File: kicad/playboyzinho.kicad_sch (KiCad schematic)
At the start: 9 parts, among them SW1 SW_SPDT, U1 esp32-s3-pl, U2 (Tela 2.8) CR2013-MI2120, U4 (Amplificador) MAX98357A I2S

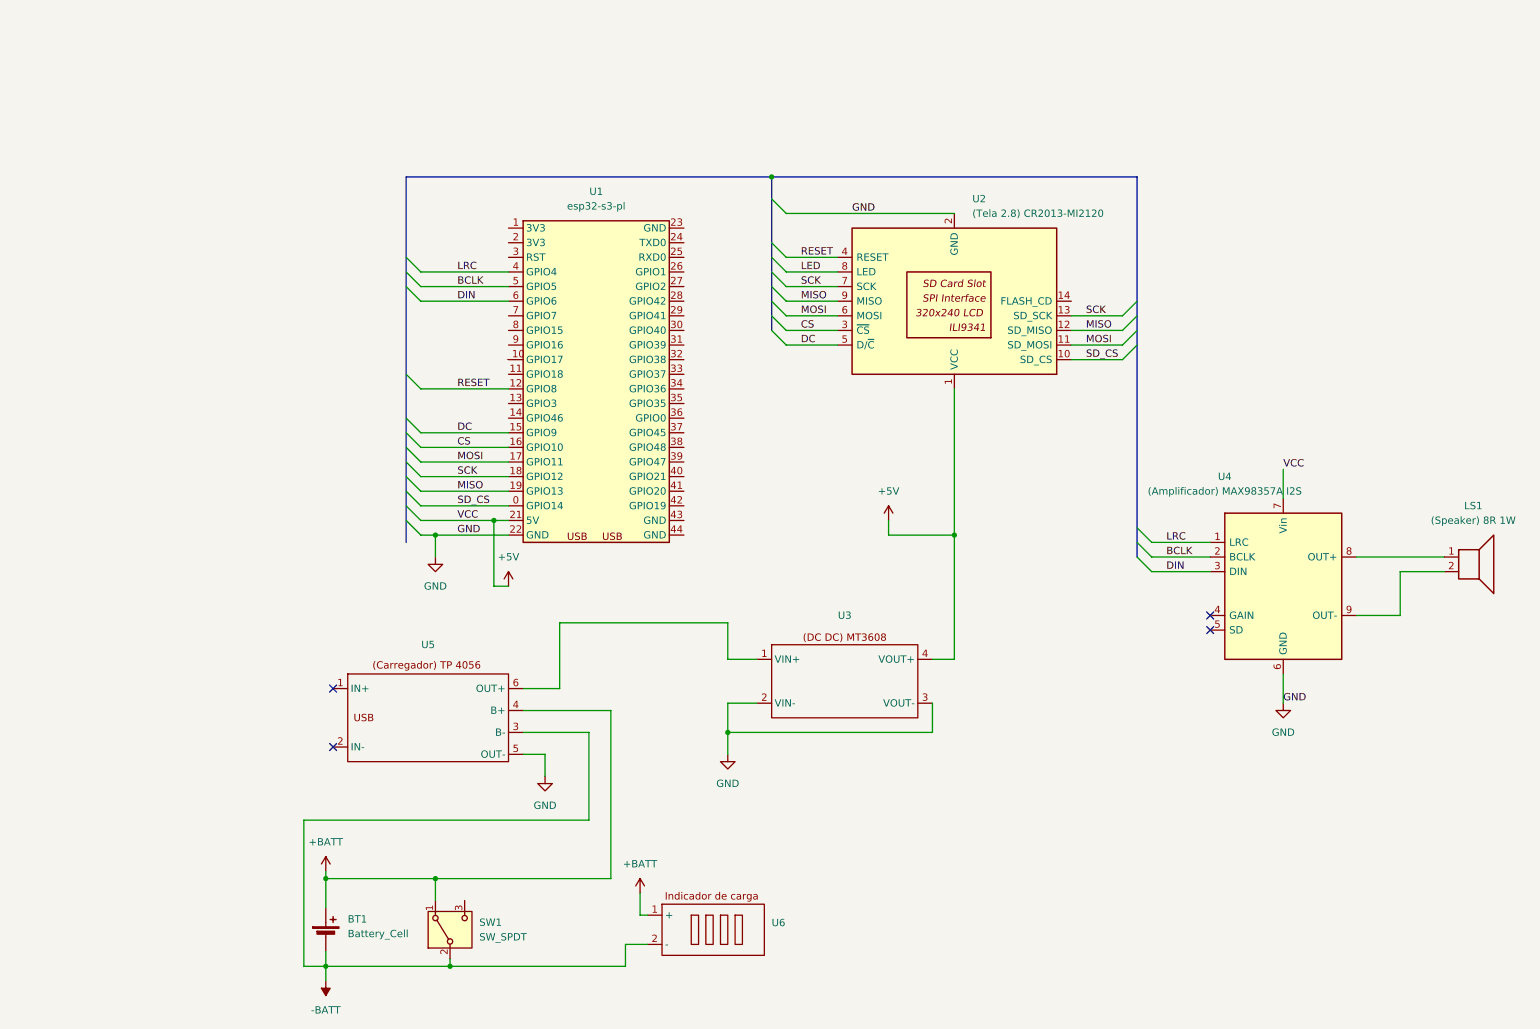
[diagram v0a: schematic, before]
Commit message: feat: adiciona lista de conexões, adiciona botões no esquemático, adiciona conexão LED que tava faltando no esquemático, remove imagens desnecessárias
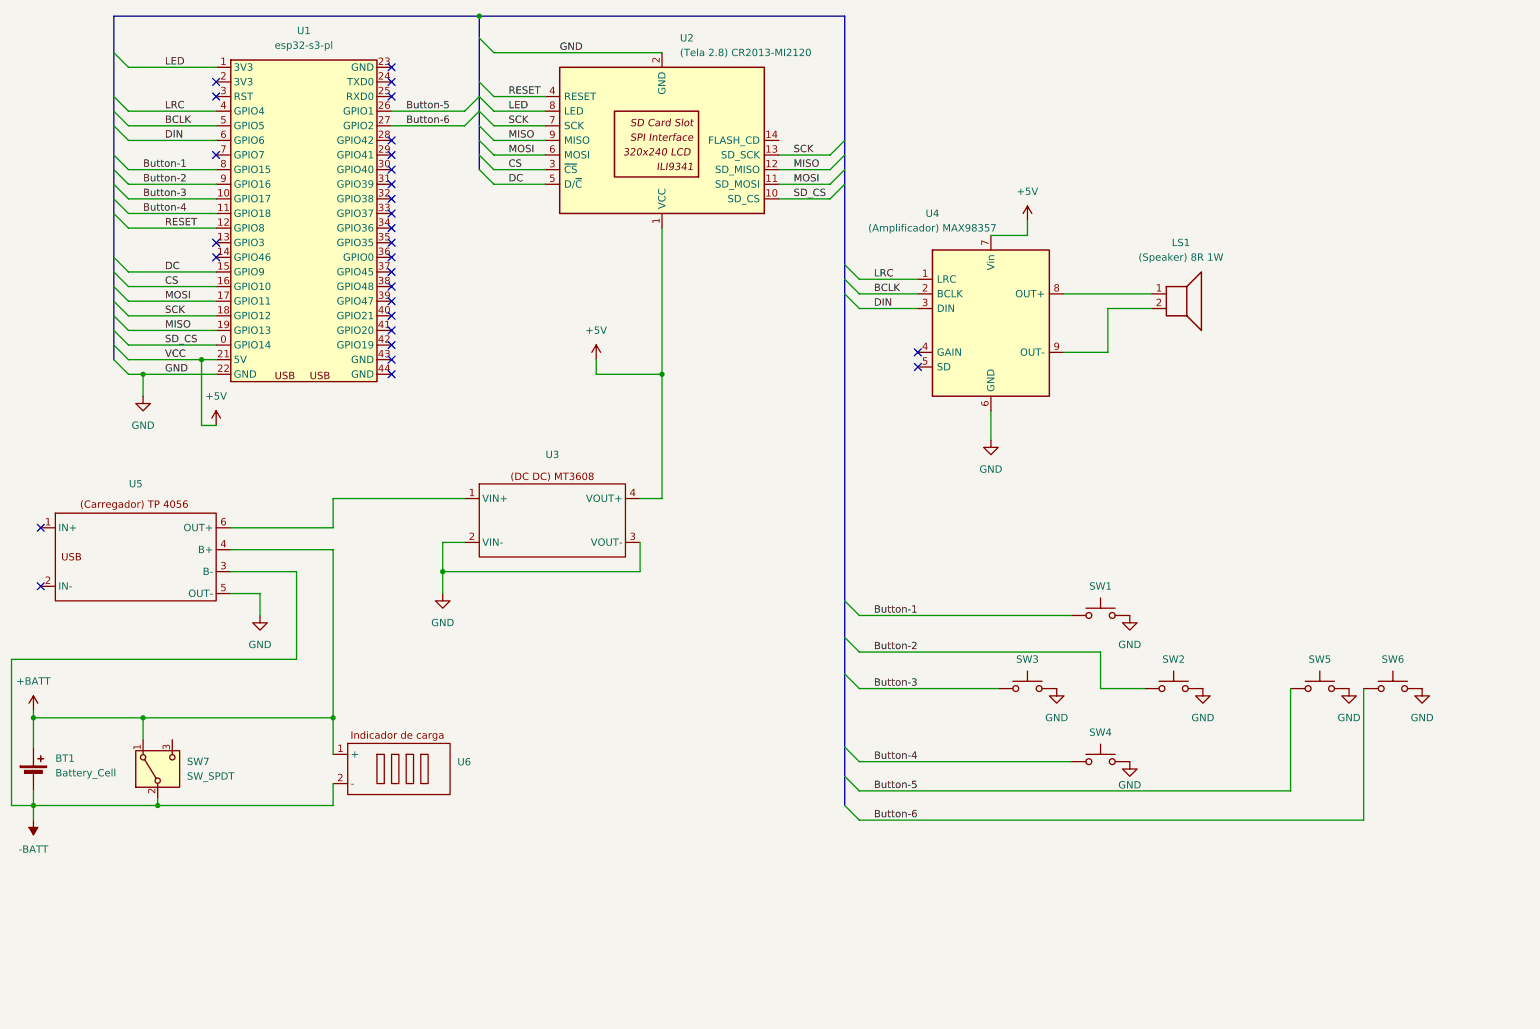
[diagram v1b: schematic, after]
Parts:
- added SW1, SW2, SW3, SW4, SW5, SW6: SW_Push, symbol Switch:SW_Push
- U4: value (Amplificador) MAX98357A I2S -> (Amplificador) MAX98357
- renumbered SW1 to SW7
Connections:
- net GND: now also SW1.2, SW2.2, SW3.2, SW4.2, SW5.2, SW6.2
- net LED: now also U1.1 (3V3)
- net Button-4: now reaches U1.11 (GPIO18)
- net Button-4: now also SW4.1
- net Button-5: now reaches U1.26 (GPIO1)
- net Button-5: now also SW5.1
- net Button-6: now reaches U1.27 (GPIO2)
- net Button-6: now also SW6.1
- net Button-1: now reaches U1.8 (GPIO15)
- net Button-1: now also SW1.1
- net Button-2: now reaches U1.9 (GPIO16)
- net Button-2: now also SW2.1
- new net Button-3: SW3.1, U1.10 (GPIO17)
- no-connect marks 4 -> 29
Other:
- moved on the sheet: BT1, LS1, SW7, U1, U2, U3, U4, U5, U6

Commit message: feat: cria novo símbolo para tela e adiciona ele no esquemático, finaliza o geralzão dos footprints (talvez precise de ajustes)
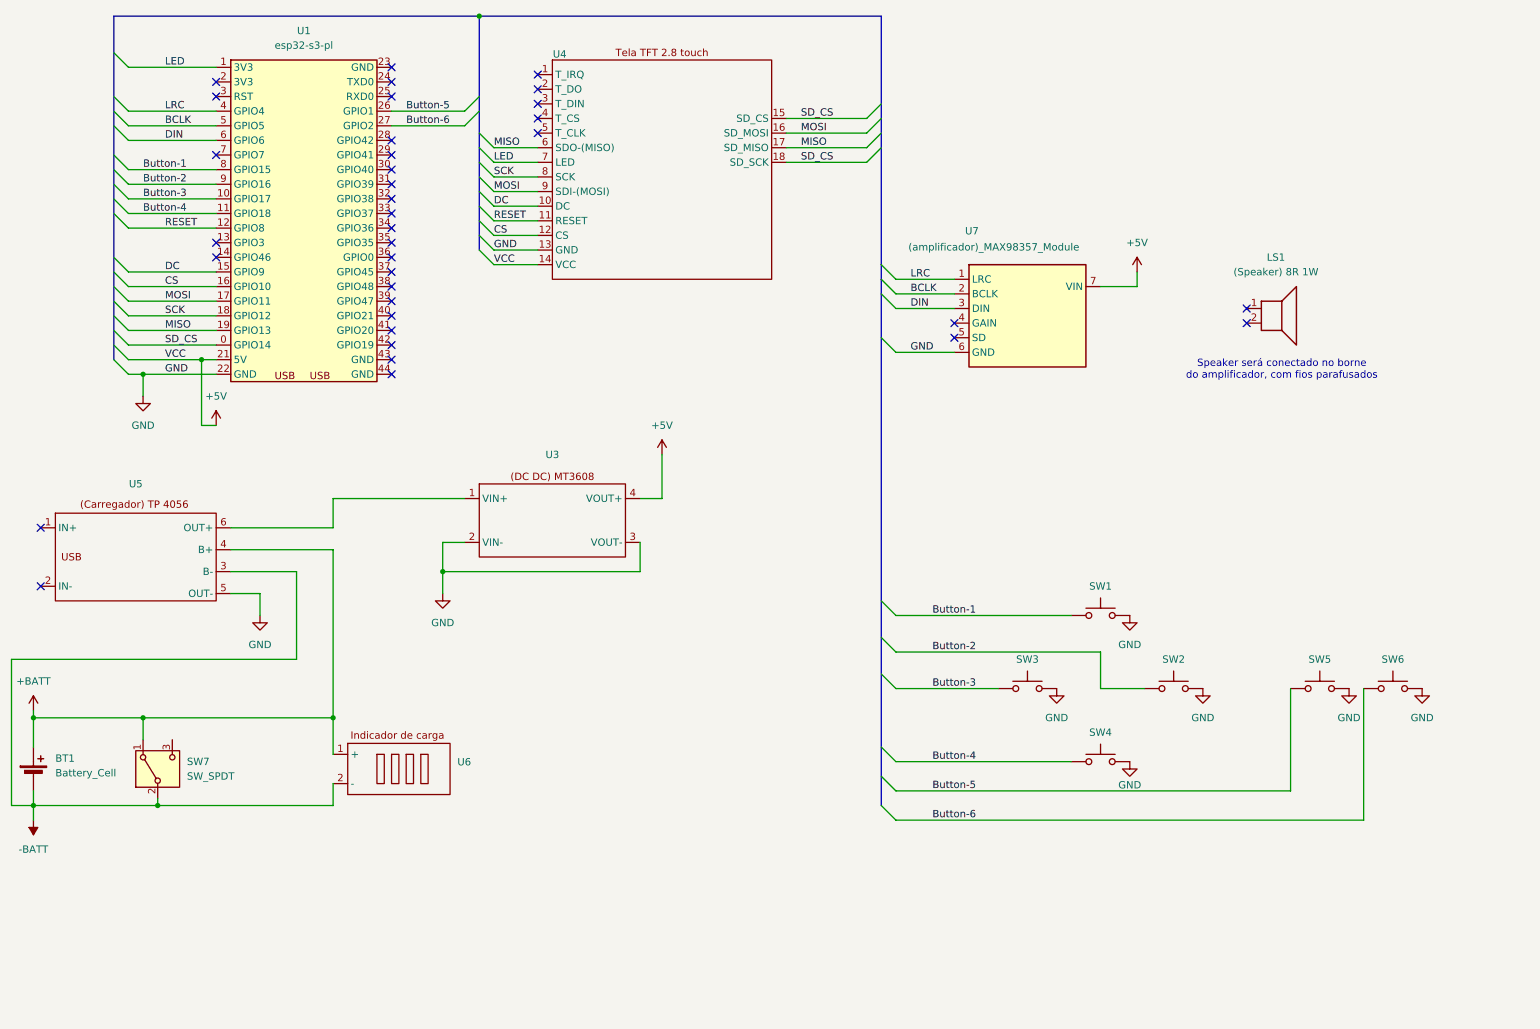
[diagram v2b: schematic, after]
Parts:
- removed U2: (Tela 2.8) CR2013-MI2120, Display:CR2013-MI2120, symbol Driver_Display:CR2013-MI2120
- removed U4: (Amplificador) MAX98357, symbol lib-do-playboy:max98357-mod
- added U4: (no value), symbol lib-do-playboy:tela-tft-2.8-touch
- added U7: (amplificador)_MAX98357_Module, Package_DFN_QFN:TQFN-16-1EP_3x3mm_P0.5mm_EP1.23x1.23mm, symbol lib-do-playboy:(amplificador)_MAX98357_Module
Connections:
- net +5V: now also U4.14 (VCC), U7.7 (VIN)
- net BCLK: now also U7.2 (BCLK)
- net CS: now also U4.12 (CS)
- net DC: now also U4.10 (DC)
- net DIN: now also U7.3 (DIN)
- net GND: now also U4.13 (GND), U7.6 (GND)
- net LED: now also U4.7 (LED)
- net LRC: now also U7.1 (LRC)
- net MISO: now also U4.17 (SD_MISO), U4.6 (SDO-(MISO))
- net MOSI: now also U4.16 (SD_MOSI), U4.9 (SDI-(MOSI))
- net RESET: now also U4.11 (RESET)
- net SCK: now also U4.8 (SCK)
- net SD_CS: now also U4.15 (SD_CS), U4.18 (SD_SCK)
- no-connect marks 29 -> 36
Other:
- note added: "Speaker será conectado no borne do amplificador, com fios parafusados"
- moved on the sheet: LS1

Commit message: feat: ajustes no esquemático, cria footprint do botão, posiciona elementos no pcb
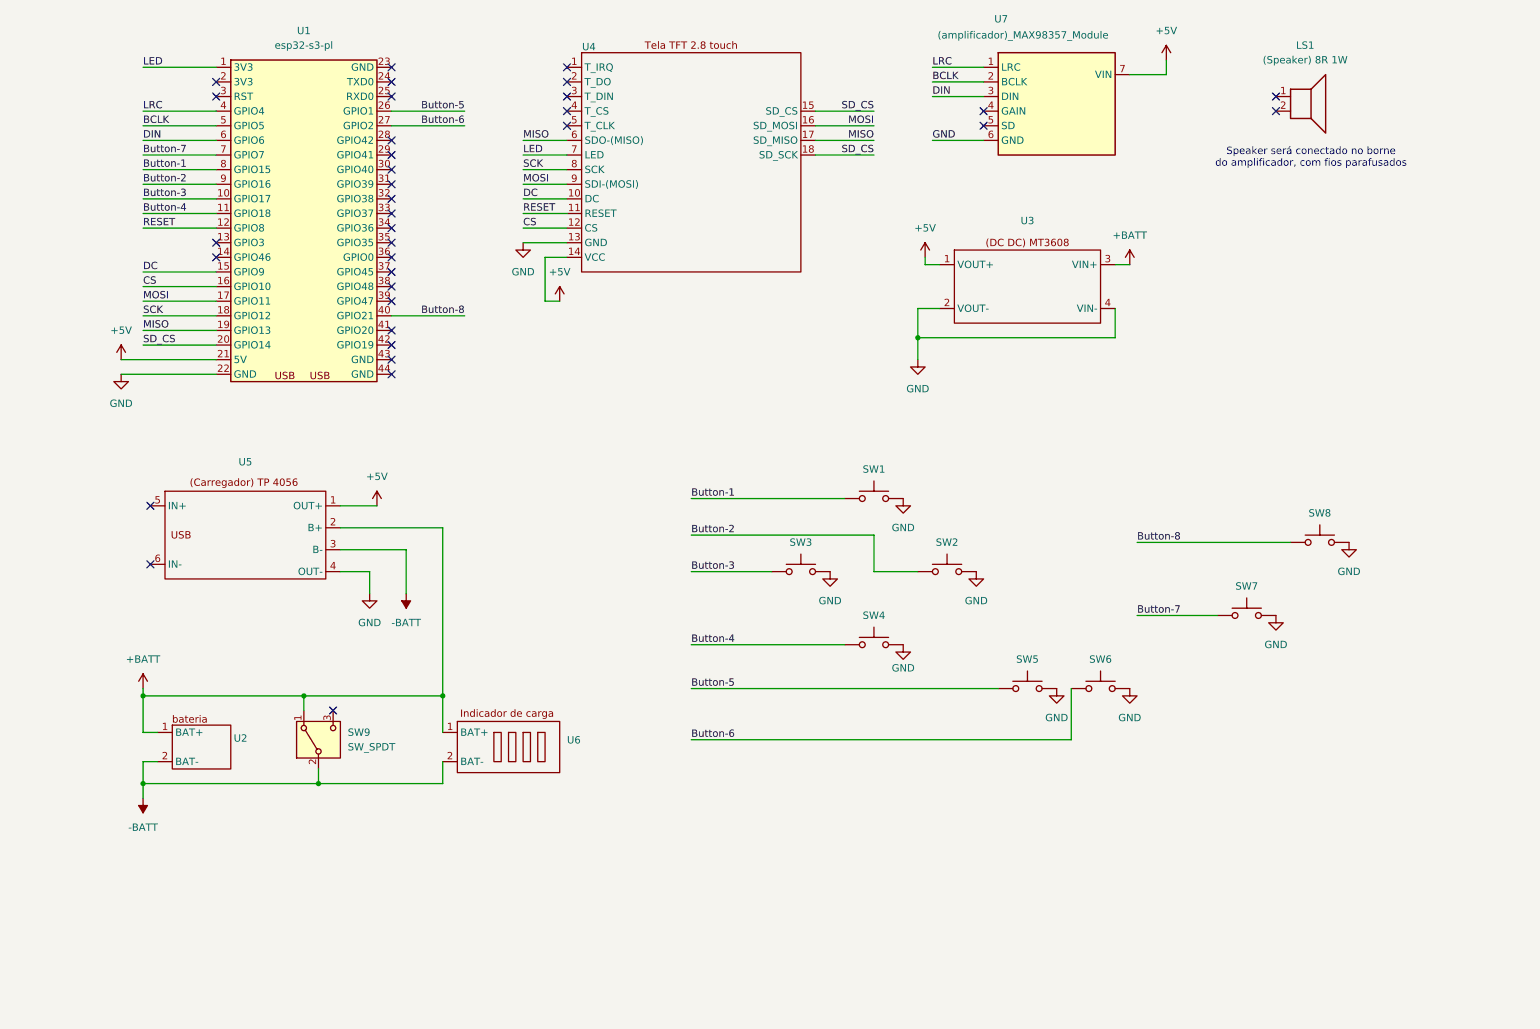
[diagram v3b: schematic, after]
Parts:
- removed BT1: Battery_Cell, Package_SON:Texas_DRC0010J_ThermalVias, symbol Device:Battery_Cell
- added SW7, SW8: SW_Push, lib-do-playboy:botao, symbol Switch:SW_Push
- added U2: (no value), symbol lib-do-playboy:bateria
- SW1, SW2, SW3, SW4, SW5, SW6: footprint (none) -> lib-do-playboy:botao
- SW9: renamed from SW7; footprint Package_SON:WSON-8-1EP_6x5mm_P1.27mm_EP3.4x4mm -> lib-do-playboy:alavanca
- U1: footprint RF_Module:ESP32-S3-WROOM-1 -> lib-do-playboy:esp32-s3
- U3: footprint Converter_DCDC:Converter_DCDC_TRACO_TSR0.5-24xx_TSR0.5-24xxx_THT -> lib-do-playboy:(dc dc) MT3608
- U4: footprint (none) -> lib-do-playboy:tela TFT 2.8
- U5: footprint Package_SO:SOIC-8-1EP_3.9x4.9mm_P1.27mm_EP2.41x3.3mm_ThermalVias -> lib-do-playboy:(carregador) TP4056
- U6: footprint (none) -> lib-do-playboy:indicador-bateria
- U7: footprint Package_DFN_QFN:TQFN-16-1EP_3x3mm_P0.5mm_EP1.23x1.23mm -> lib-do-playboy:(amplificador) MAX98357_Module
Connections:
- net +5V: now also U3.1 (VOUT+), U5.1 (OUT+); no longer U3.4 (VOUT+)
- net +BATT: now also U3.3 (VIN+), U5.2 (B+), U2.1 (BAT+); no longer U5.4 (B+)
- net -BATT: now also U2.2 (BAT-)
- net GND: now also U3.4 (VIN-), U5.4 (OUT-), SW7.2, SW8.2; no longer U3.3 (VOUT-), U5.5 (OUT-)
- net SD_CS: now also U1.20 (GPIO14); no longer U1.0 (GPIO14)
- net at U5.6 (IN-): no longer U3.1 (VIN+)
- net Button-8: now reaches U1.40 (GPIO21)
- net Button-8: now also SW8.1
- net Button-7: now reaches U1.7 (GPIO7)
- net Button-7: now also SW7.1
- no-connect marks 36 -> 35
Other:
- moved on the sheet: LS1, SW1, SW2, SW3, SW4, SW5, SW6, SW9, U3, U4, U5, U6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

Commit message: fix: corrige conexões do esquemático e direção dos pinos de determinados símbolos
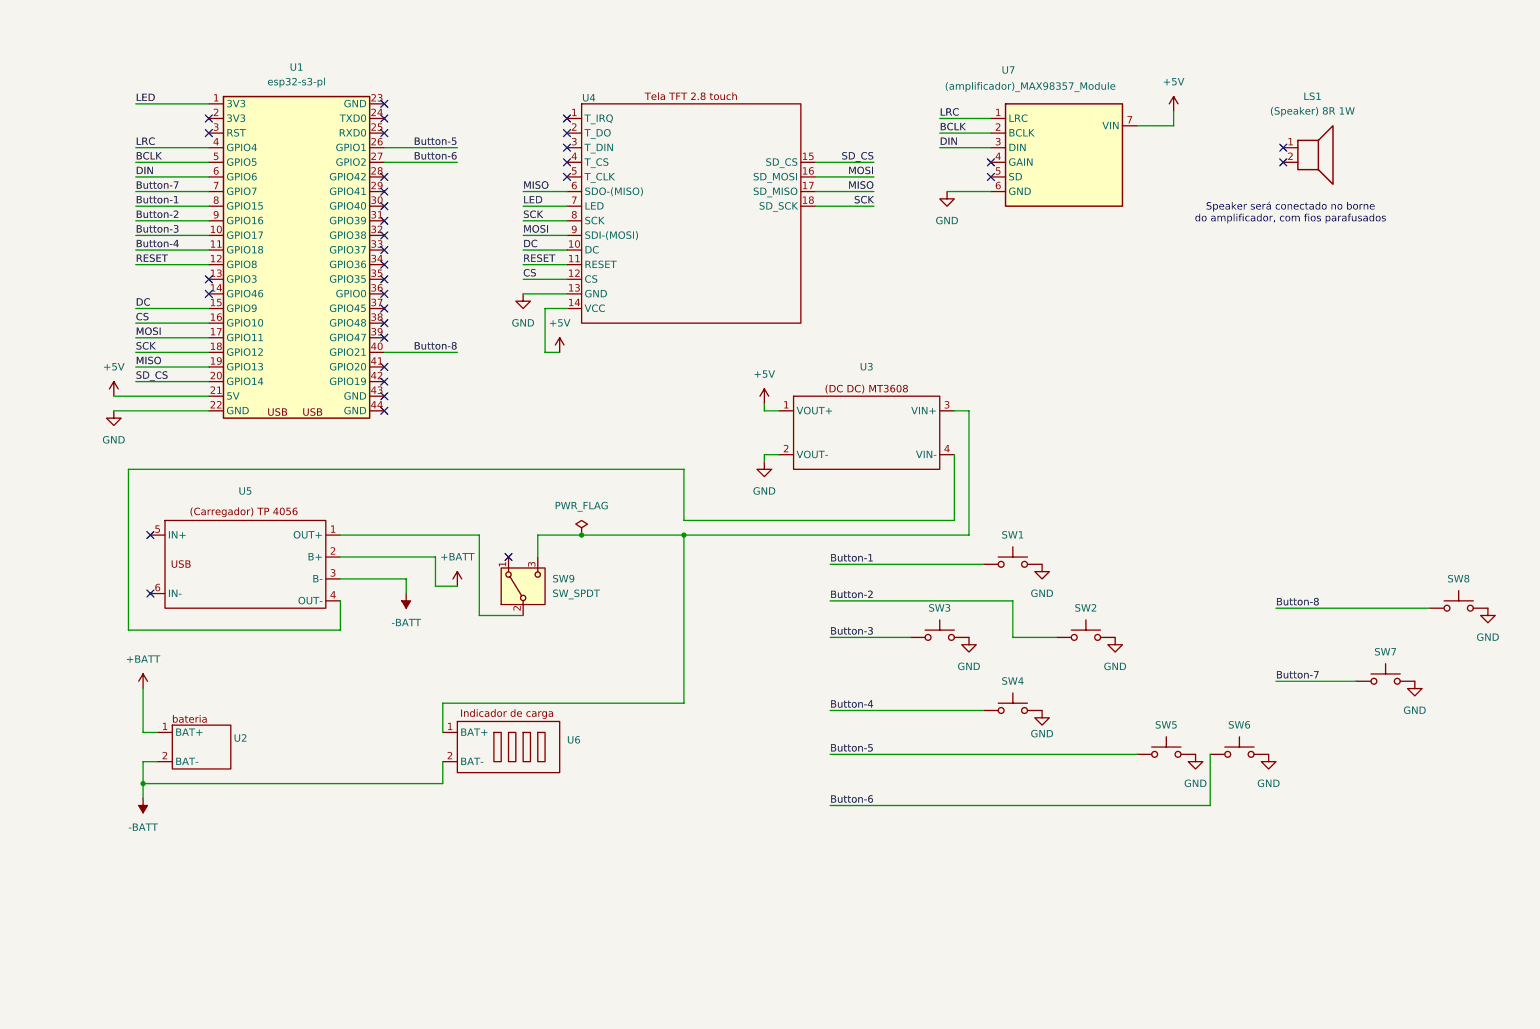
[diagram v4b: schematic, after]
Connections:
- net +5V: no longer U5.1 (OUT+)
- net +BATT: no longer SW9.1 (A), U3.3 (VIN+), U6.1 (BAT+)
- net -BATT: no longer SW9.2 (B)
- net GND: no longer U3.4 (VIN-), U5.4 (OUT-)
- net SCK: now also U4.18 (SD_SCK)
- net SD_CS: no longer U4.18 (SD_SCK)
- net at SW9.3 (C): now also U3.3 (VIN+), U6.1 (BAT+)
- new net: U3.4 (VIN-), U5.4 (OUT-)
- new net: SW9.2 (B), U5.1 (OUT+)
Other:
- moved on the sheet: LS1, SW1, SW2, SW3, SW4, SW5, SW6, SW7, SW8, SW9, U1, U3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
